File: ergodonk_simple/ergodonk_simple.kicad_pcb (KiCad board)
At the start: 2 copper layers, 216.6 x 155.6 mm, 142 parts, among them J10 Pimaroni Trackball, J11 4PIN, J12 Conn_01x08_Socket, Q1 TIP120, SW0 SW_PUSH_LED, SW08_RH10 SW_PUSH_LED, SW1 SW_PUSH_LED, SW10 SW_PUSH_LED, SW11 SW_PUSH_LED, SW12 SW_PUSH_LED, SW13 SW_PUSH_LED, SW14 SW_PUSH_LED, SW15 SW_PUSH_LED, SW16 SW_PUSH_LED, SW17 SW_PUSH_LED, SW18 RotaryEncoder, SW18_RH10 SW_PUSH_LED, SW2 SW_PUSH_LED, SW20 SW_PUSH_LED, SW21 SW_PUSH_LED, SW22 SW_PUSH_LED, SW23 SW_PUSH_LED, SW24 SW_PUSH_LED, SW25 SW_PUSH_LED, SW26 SW_PUSH_LED, SW27 SW_PUSH_LED, SW28_RH10 SW_PUSH_LED, SW3 SW_PUSH_LED, SW30 SW_PUSH_LED, SW31 SW_PUSH_LED, SW32 SW_PUSH_LED, SW33 SW_PUSH_LED, SW34 SW_PUSH_LED, SW35 SW_PUSH_LED, SW36 SW_PUSH_LED, SW37 SW_PUSH_LED, SW38_RH10 SW_PUSH_LED, SW4 SW_PUSH_LED, SW40 SW_PUSH_LED, SW42 SW_PUSH_LED, SW43 SW_PUSH_LED, SW44 SW_PUSH_LED, SW45 SW_PUSH_LED, SW46 SW_PUSH_LED, SW47 SW_PUSH_LED, SW48_RH10 SW_PUSH_LED, SW5 SW_PUSH_LED, SW50 SW_PUSH_LED, SW51 SW_PUSH_LED, SW52 SW_PUSH_LED, SW53 SW_PUSH_LED, SW54 SW_PUSH_LED, SW55 SW_PUSH_LED, SW56 SW_PUSH_LED, SW57 SW_PUSH_LED, SW58 SW_PUSH_LED, SW6 SW_PUSH_LED, SW7 SW_PUSH_LED, U11 Pico

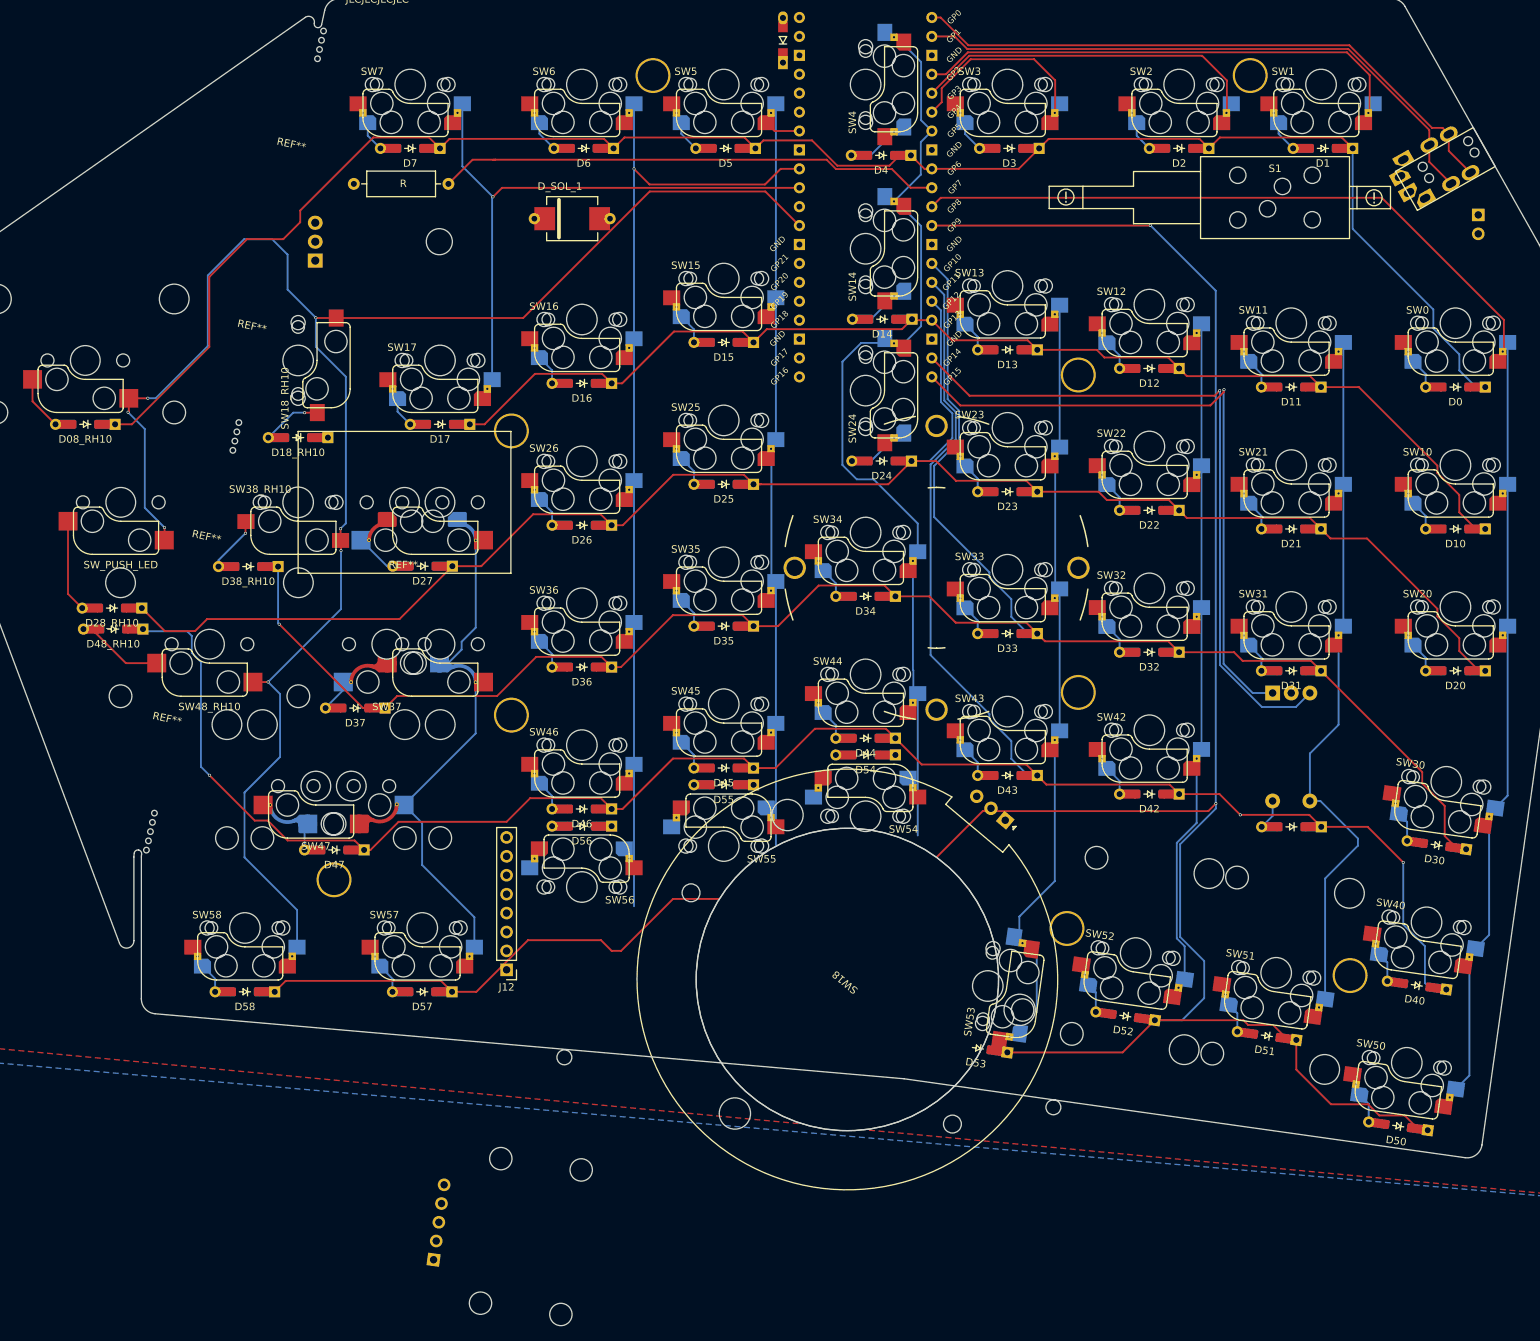
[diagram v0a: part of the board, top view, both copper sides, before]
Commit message: Flipped rotary encoder to backside
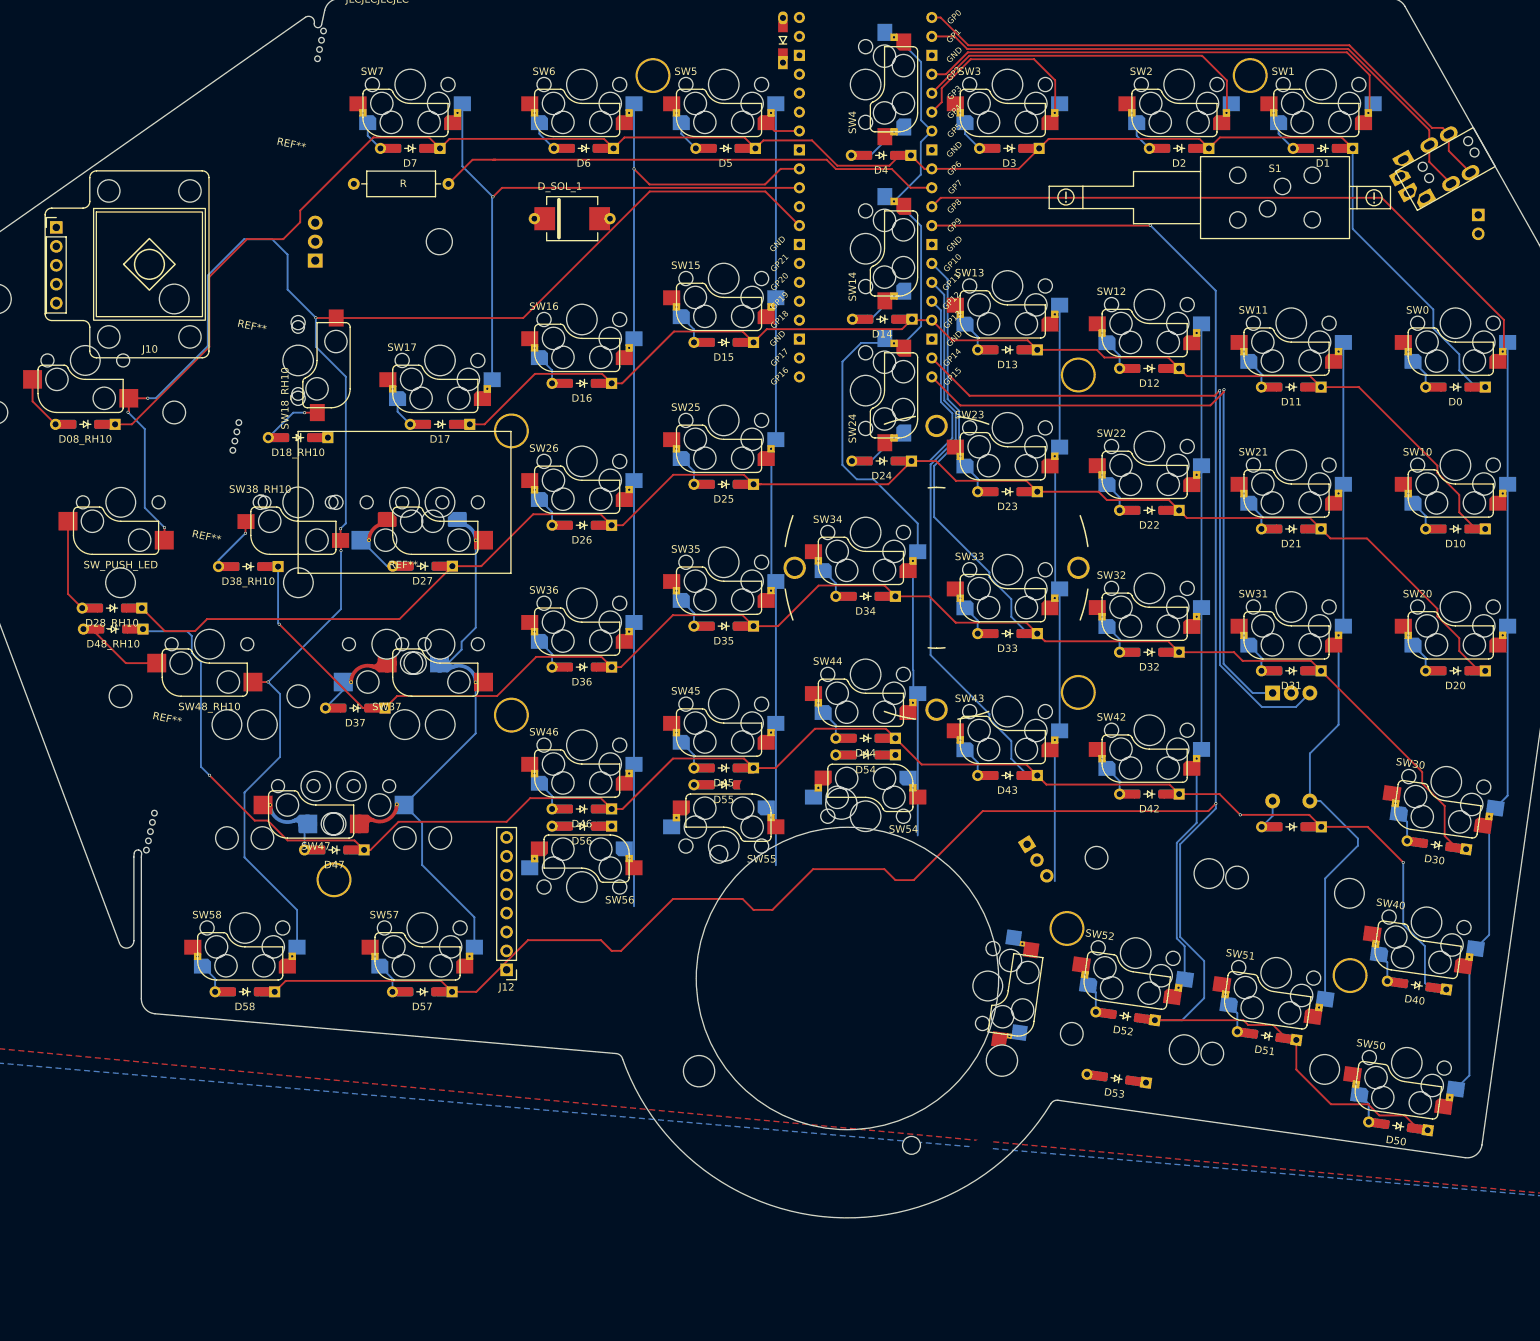
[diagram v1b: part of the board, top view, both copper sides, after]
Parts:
- J10: moved to F.Cu
- SW0, SW1, SW10, SW11, SW12, SW13, SW14, SW15, SW16, SW17, SW2, SW20, SW21, SW22, SW23, SW24, SW25, SW26, SW3, SW30, SW31, SW32, SW33, SW34, SW35, SW36, SW4, SW40, SW42, SW43, SW44, SW45, SW46, SW5, SW50, SW51, SW52, SW54, SW55, SW56, SW57, SW58, SW6, SW7: footprint ergodonk_pico:Cherry_MX_DS_Hotswap_1U_sofle3b v2 -> ergodonk_simple:Cherry_MX_DS_Hotswap_1U_sofle3b v3
- SW18: moved to B.Cu
- SW53: footprint ergodonk_pico:Cherry_MX_DS_Hotswap_1U_sofle3b v2 -> ergodonk_simple:CherryMX_Choc_Hotswap; moved to B.Cu
- moved J10 147.6 mm to (52.2, 53.0), turned to 0 degrees
- moved D53 19.1 mm to (194.6, 167.3)
- moved SW18 0.13 mm to (158.4, 153.8), turned to -58 degrees
- turned SW53 to 82 degrees
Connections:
- SW53 pad 5: Net-(D53-A) -> (no net)
- SW53 pad 6: col3 -> (no net)
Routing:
- net row5: track 355.0 -> 333.4 mm
- net col3: track 122.9 -> 102.3 mm
- net Net-(D53-A): track 3.97 -> 0.00 mm
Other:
- board size 216.6 x 155.6 mm -> 216.6 x 163.7 mm
